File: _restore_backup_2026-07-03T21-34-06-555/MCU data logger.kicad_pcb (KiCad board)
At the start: 2 copper layers, 53.1 x 35.5 mm, 29 parts, among them J1 Conn_01x04_Pin, J2 Conn_01x04_Pin, J3 Conn_01x09_Pin, J4 Conn_02x03_Odd_Even, U1 ATMEGA328P-AN, U2 DS1337S_, U3 24LC1025, U4 24LC1025, Y1 32.768Khz, Y2 16MHz

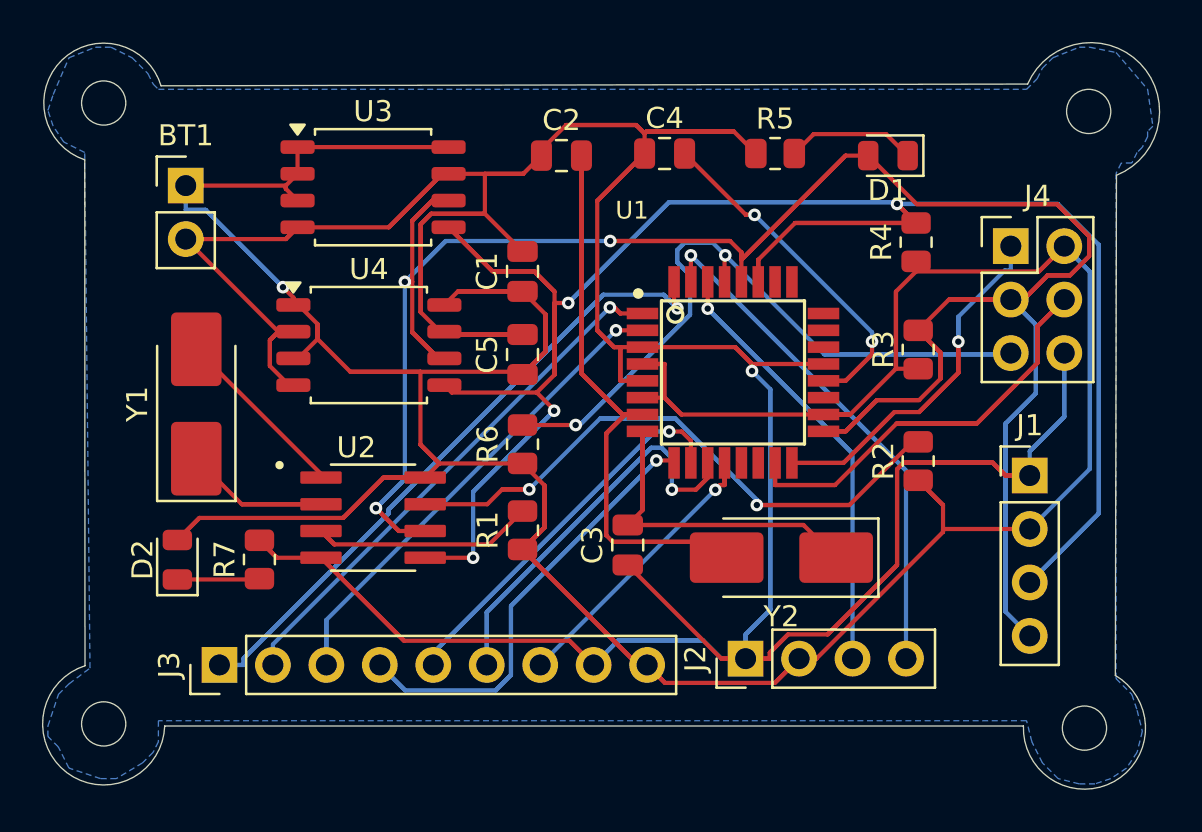
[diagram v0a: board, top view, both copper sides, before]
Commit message: Completed 2-layer PCB layout
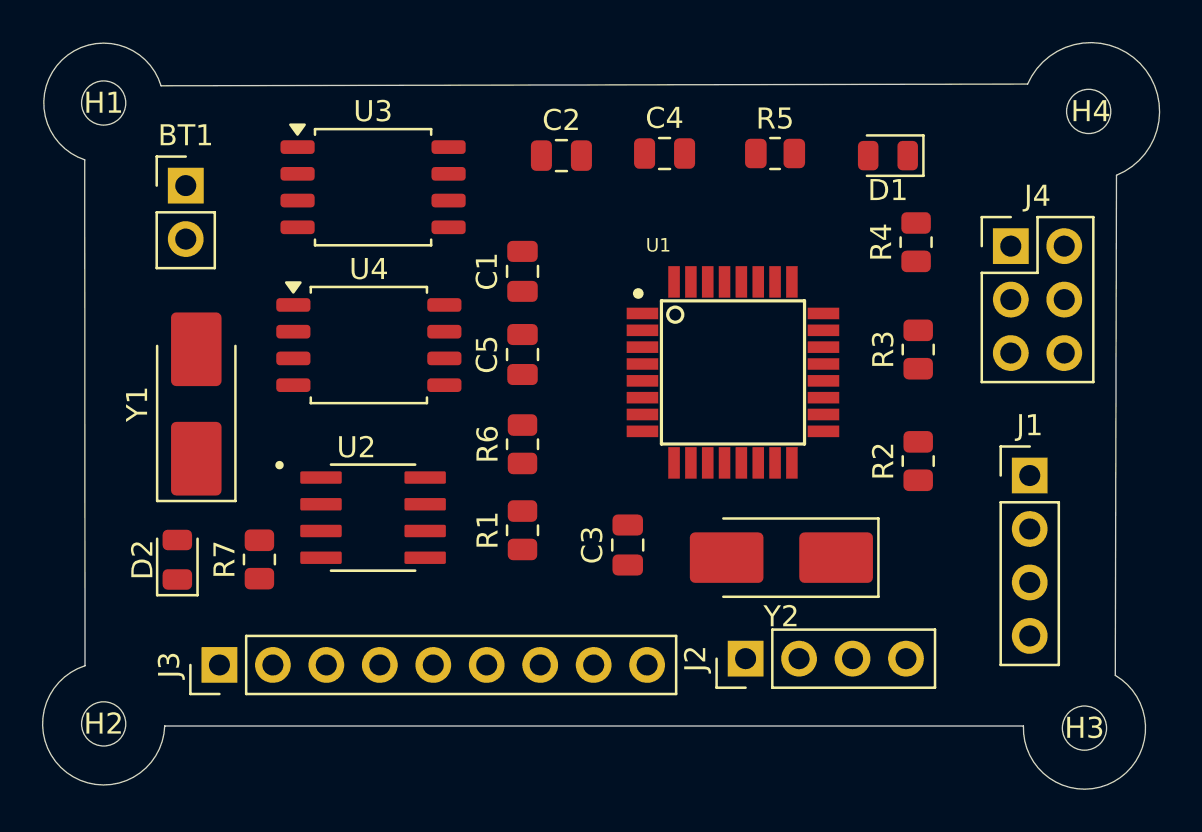
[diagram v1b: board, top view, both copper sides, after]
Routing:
- net GND: track 246.7 -> 0.00 mm, vias 1 -> 0
- net VCC: track 213.4 -> 0.00 mm, vias 1 -> 0
- net /sck: track 164.5 -> 0.00 mm, vias 3 -> 0
- net /sda: track 150.5 -> 0.00 mm, vias 4 -> 0
- net /D2: track 57.7 -> 0.00 mm, vias 1 -> 0
- net /RESET: track 54.6 -> 0.00 mm, vias 2 -> 0
- net Net-(U1-PB6): track 54.2 -> 0.00 mm
- net Net-(U2-SQW/~INT): track 43.4 -> 0.00 mm, vias 2 -> 0
- net /TX: track 39.1 -> 0.00 mm, vias 1 -> 0
- net /D5: track 36.8 -> 0.00 mm, vias 1 -> 0
- net /D7: track 35.1 -> 0.00 mm, vias 1 -> 0
- net /MOSI: track 34.8 -> 0.00 mm
- net /D6: track 33.9 -> 0.00 mm, vias 1 -> 0
- net /RX: track 30.5 -> 0.00 mm, vias 1 -> 0
- net /MISO: track 28.1 -> 0.00 mm, vias 1 -> 0
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- removed copper zone on B.Cu, net GND
